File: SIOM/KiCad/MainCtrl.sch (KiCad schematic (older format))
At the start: 6 parts, among them SW901 SW_Push, U901 TinyPico

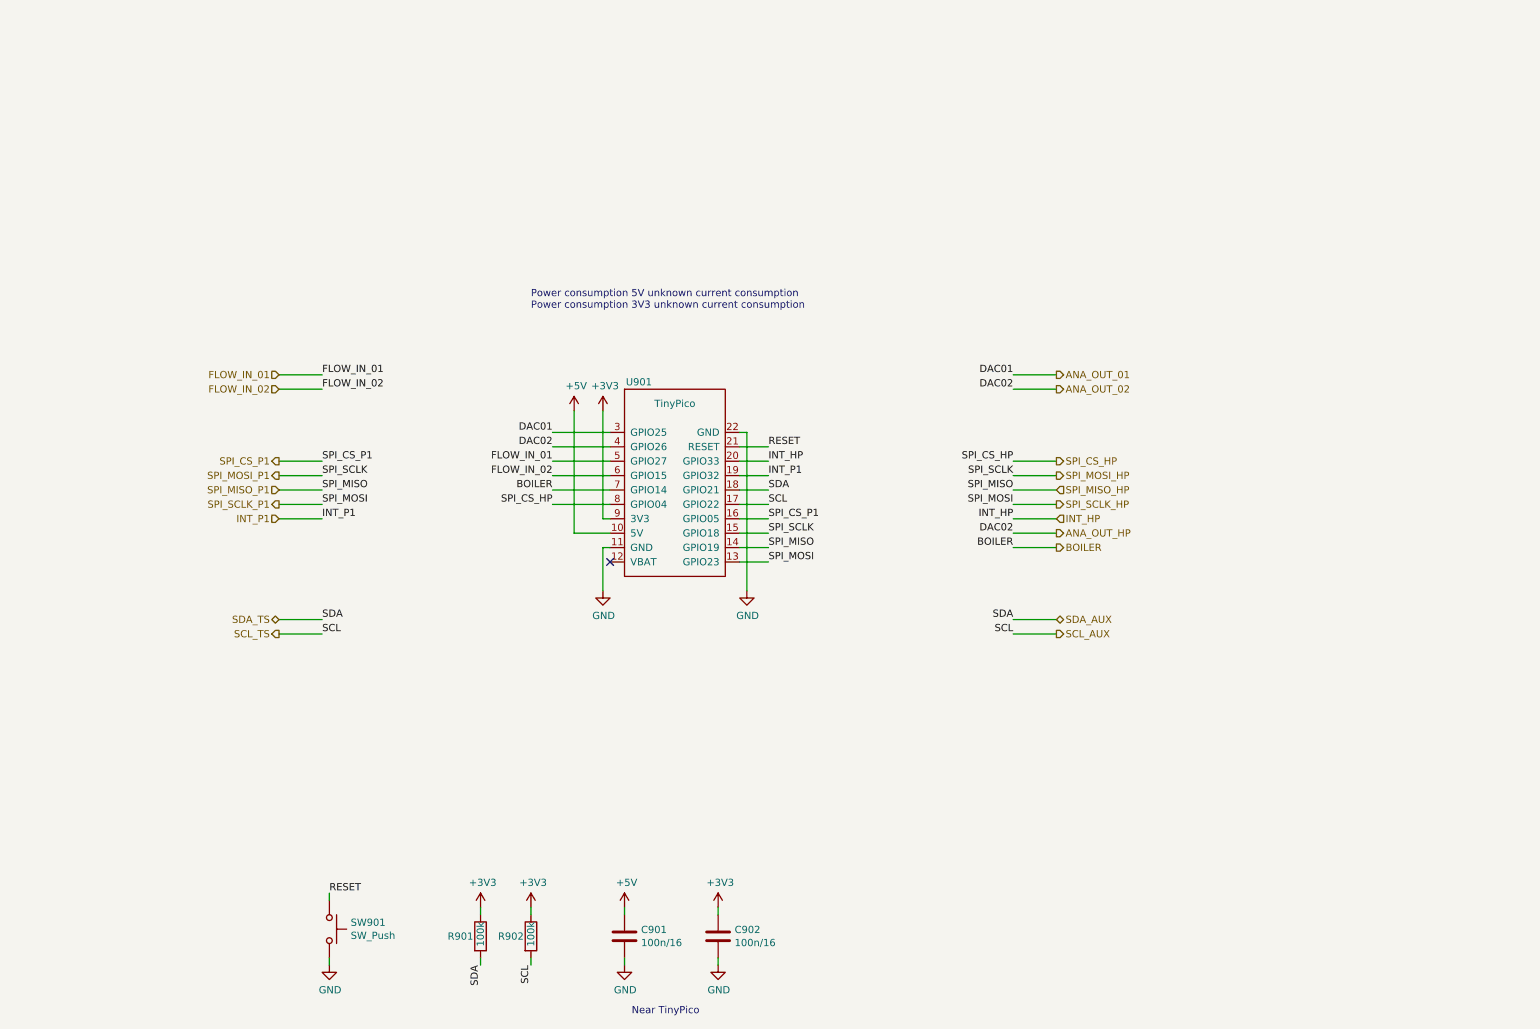
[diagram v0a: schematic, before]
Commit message: KiCad files SIOM_def
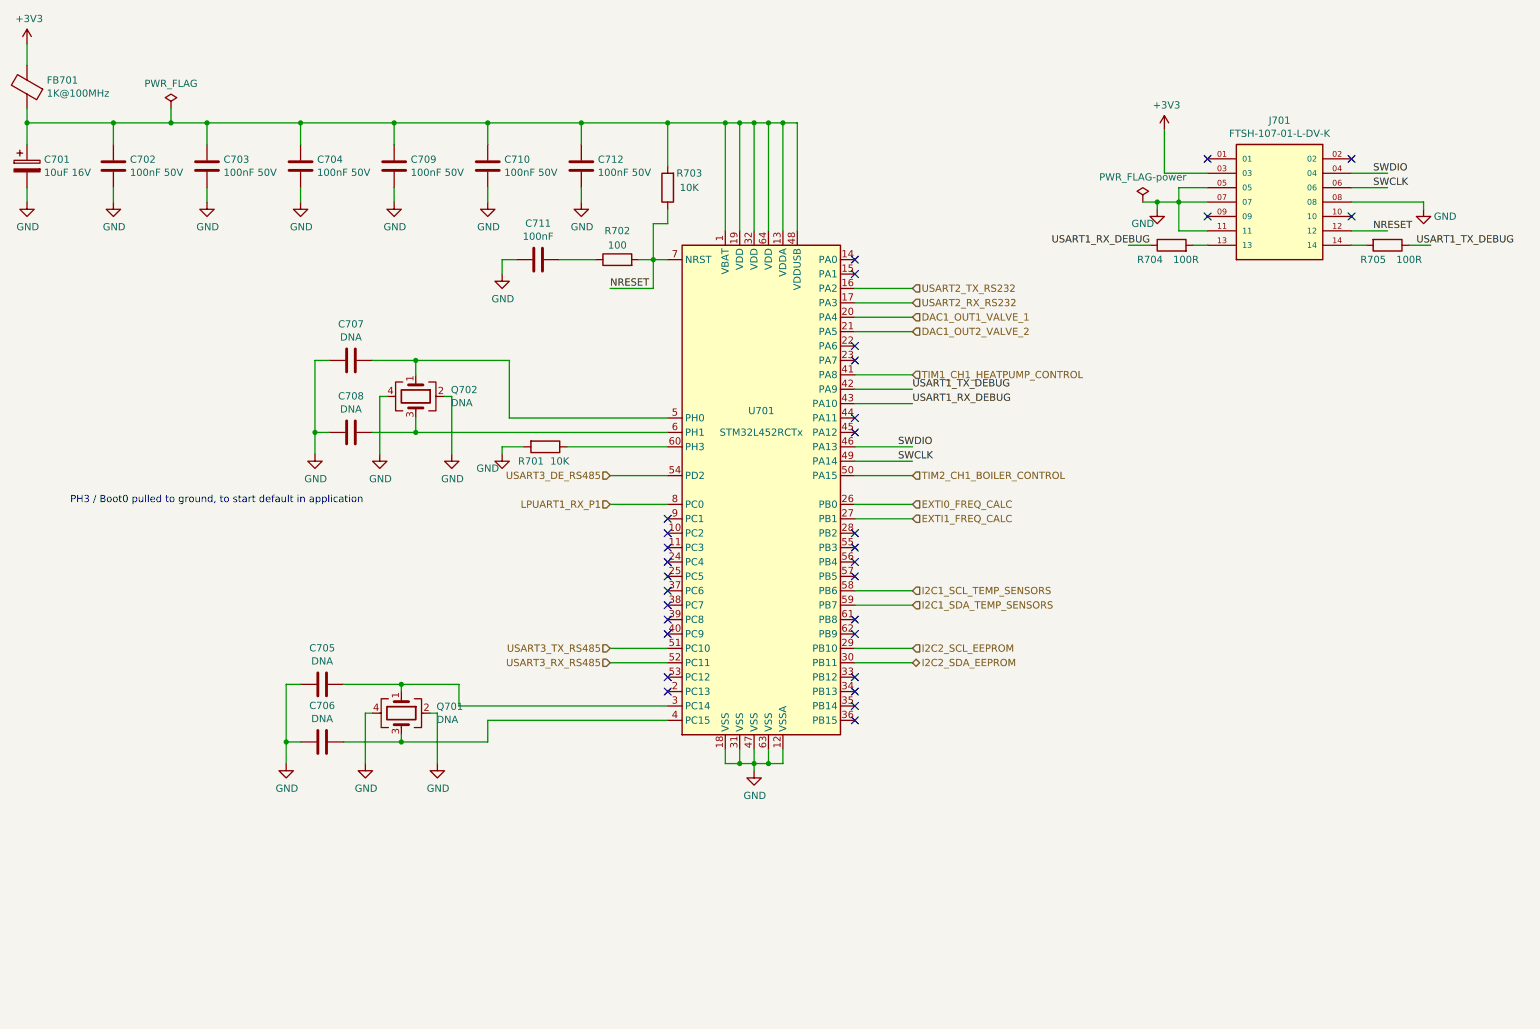
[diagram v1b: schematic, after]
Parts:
- removed C901, C902: 100n/16, Capacitor_SMD:C_0603_1608Metric, symbol SIOMv01-rescue:C-Device
- removed R901, R902: 100k, Resistor_SMD:R_0603_1608Metric, symbol SIOMv01-rescue:R-Device
- removed SW901: SW_Push, Button_Switch_SMD:SW_Push_1P1T_NO_6x6mm_H9.5mm, symbol Switch:SW_Push
- removed U901: TinyPico, Package_DIP:DIP-24_W15.24mm_Socket_LongPads, symbol TinyPico:TinyPico
- added C701: 10uF 16V, Capacitor_SMD:C_1206_3216Metric_Pad1.33x1.80mm_HandSolder, symbol Device:CP
- added C702, C703, C704, C709, C710, C712: 100nF 50V, Capacitor_SMD:C_0603_1608Metric, symbol Device:C
- added C705, C706, C707, C708: DNA, Capacitor_SMD:C_0603_1608Metric_Pad1.08x0.95mm_HandSolder, symbol Device:C
- added C711: 100nF, Capacitor_SMD:C_0603_1608Metric, symbol Device:C
- added FB701: 1K@100MHz, Resistor_SMD:R_0603_1608Metric_Pad0.98x0.95mm_HandSolder, symbol Device:Ferrite_Bead
- added J701: FTSH-107-01-L-DV-K, FTSH:SAMTEC_FTSH-107-01-L-DV-K, symbol FTSH:FTSH-107-01-L-DV-K
- added Q701, Q702: DNA, Crystal:Crystal_SMD_Abracon_ABM8G-4Pin_3.2x2.5mm, symbol Device:Crystal_GND24
- added R701, R703: 10K, Resistor_SMD:R_0603_1608Metric, symbol Device:R
- added R702: 100, Resistor_SMD:R_0603_1608Metric, symbol Device:R
- added R704, R705: 100R, Resistor_SMD:R_0603_1608Metric, symbol Device:R
- added U701: STM32L452RCTx, Package_QFP:LQFP-64_10x10mm_P0.5mm, symbol MCU_ST_STM32L4:STM32L452RCTx
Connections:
- net labels added: DAC1_OUT1_VALVE_1, DAC1_OUT2_VALVE_2, EXTI0_FREQ_CALC, EXTI1_FREQ_CALC, I2C1_SCL_TEMP_SENSORS, I2C1_SDA_TEMP_SENSORS, I2C2_SCL_EEPROM, I2C2_SDA_EEPROM, LPUART1_RX_P1, NRESET, SWCLK, SWDIO, TIM1_CH1_HEATPUMP_CONTROL, TIM2_CH1_BOILER_CONTROL, USART1_RX_DEBUG, USART1_TX_DEBUG, USART2_RX_RS232, USART2_TX_RS232, USART3_DE_RS485, USART3_RX_RS485, USART3_TX_RS485
- net labels removed: +5V, ANA_OUT_01, ANA_OUT_02, ANA_OUT_HP, BOILER, DAC01, DAC02, FLOW_IN_01, FLOW_IN_02, INT_HP, INT_P1, RESET, SCL, SCL_AUX, SCL_TS, SDA, SDA_AUX, SDA_TS, SPI_CS_HP, SPI_CS_P1, SPI_MISO, SPI_MISO_HP, SPI_MISO_P1, SPI_MOSI, SPI_MOSI_HP, SPI_MOSI_P1, SPI_SCLK, SPI_SCLK_HP, SPI_SCLK_P1
- wire segments 53 -> 134
- no-connect marks 1 -> 31
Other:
- note added: "PH3 / Boot0 pulled to ground, to start default in application"
- note removed: "Near TinyPico"
- note removed: "Power consumption 5V unknown current consumption\nPower consumption 3V3 unknown current consumption"
